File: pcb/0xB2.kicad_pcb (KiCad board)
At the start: 2 copper layers, 17.8 x 33 mm, 42 parts, among them J1 USB_C_Receptacle_USB2.0, J2 Conn_01x12, J3 Conn_01x05, J4 Conn_01x12, J5 Conn_01x02, SW1 SW_Push, SW2 SW_Push, U1 RP2040, U2 GD25Q80CEIGR, U3 XC6210B332MR-G, Y1 Crystal_GND24

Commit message: import
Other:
- board size 17.8 x 33 mm -> 41.8 x 50.8 mm
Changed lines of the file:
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@@
       (xy 149.2 92.45)
     ) (layer "F.SilkS") (width 0.15) (fill solid))
-  (gr_line (start 143.51 107.95) (end 143.51 77.47) (layer "Edge.Cuts") (width 0.1))
-  (gr_line (start 148.05 81.35) (end 149.25 81.35) (layer "Edge.Cuts") (width 0.1))
-  (gr_arc (start 155.55 81.75) (mid 155.491421 81.891421) (end 155.35 81.95) (layer "Edge.Cuts") (width 0.1))
-  (gr_line (start 156.95 81.15) (end 156.95 76.2) (layer "Edge.Cuts") (width 0.1))
-  (gr_arc (start 161.29 107.95) (mid 160.918026 108.848026) (end 160.02 109.22) (layer "Edge.Cuts") (width 0.1))
-  (gr_line (start 147.85 76.2) (end 147.85 81.15) (layer "Edge.Cuts") (width 0.1))
-  (gr_arc (start 144.78 109.22) (mid 143.881974 108.848026) (end 143.51 107.95) (layer "Edge.Cuts") (width 0.1))
-  (gr_arc (start 156.95 81.15) (mid 156.891421 81.291421) (end 156.75 81.35) (layer "Edge.Cuts") (width 0.1))
-  (gr_line (start 149.25 81.35) (end 149.25 81.75) (layer "Edge.Cuts") (width 0.1))
-  (gr_line (start 161.29 77.47) (end 161.29 107.95) (layer "Edge.Cuts") (width 0.1))
-  (gr_line (start 160.02 109.22) (end 144.78 109.22) (layer "Edge.Cuts") (width 0.1))
-  (gr_line (start 144.78 76.2) (end 147.85 76.2) (layer "Edge.Cuts") (width 0.1))
-  (gr_line (start 155.55 81.75) (end 155.55 81.35) (layer "Edge.Cuts") (width 0.1))
-  (gr_arc (start 149.45 81.95) (mid 149.308579 81.891421) (end 149.25 81.75) (layer "Edge.Cuts") (width 0.1))
-  (gr_line (start 156.95 76.2) (end 160.02 76.2) (layer "Edge.Cuts") (width 0.1))
-  (gr_arc (start 148.05 81.35) (mid 147.908579 81.291421) (end 147.85 81.15) (layer "Edge.Cuts") (width 0.1))
-  (gr_arc (start 160.02 76.2) (mid 160.918026 76.571974) (end 161.29 77.47) (layer "Edge.Cuts") (width 0.1))
-  (gr_line (start 155.55 81.35) (end 156.75 81.35) (layer "Edge.Cuts") (width 0.1))
-  (gr_arc (start 143.51 77.47) (mid 143.881974 76.571974) (end 144.78 76.2) (layer "Edge.Cuts") (width 0.1))
-  (gr_line (start 149.45 81.95) (end 155.35 81.95) (layer "Edge.Cuts") (width 0.1))
+  (gr_arc (start 150.323649 128.768354) (mid 149.285 128.335) (end 148.86165 127.292233) (layer "Edge.Cuts") (width 0.2))
+  (gr_arc (start 174.953514 106.488749) (mid 177.10863 111.211774) (end 173.011529 114.400074) (layer "Edge.Cuts") (width 0.2))
+  (gr_line (start 161.993697 78.84806) (end 138.649352 78.809096) (layer "Edge.Cuts") (width 0.2))
+  (gr_line (start 171.173514 77.998749) (end 163.855 78.015) (layer "Edge.Cuts") (width 0.2))
+  (gr_arc (start 162.955 78.415) (mid 163.367804 78.13131) (end 163.855 78.015) (layer "Edge.Cuts") (width 0.1))
+  (gr_line (start 150.323649 128.768354) (end 165.179642 128.797362) (layer "Edge.Cuts") (width 0.2))
+  (gr_arc (start 174.953514 106.488749) (mid 173.241074 104.864213) (end 172.613514 102.588749) (layer "Edge.Cuts") (width 0.2))
+  (gr_arc (start 135.454058 82.315) (mid 136.31466 79.890303) (end 138.649352 78.809096) (layer "Edge.Cuts") (width 0.2))
+  (gr_arc (start 166.652176 127.348393) (mid 166.216517 128.378374) (end 165.179642 128.797362) (layer "Edge.Cuts") (width 0.2))
+  (gr_line (start 148.885 113.835) (end 148.858709 117.290003) (layer "Edge.Cuts") (width 0.1))
+  (gr_line (start 141.724995 91.687466) (end 141.724995 96.446645) (layer "Edge.Cuts") (width 0.1))
+  (gr_arc (start 138.908049 87.137466) (mid 140.993806 88.993153) (end 141.724995 91.687466) (layer "Edge.Cuts") (width 0.2))
+  (gr_arc (start 144.085 110.835) (mid 142.403633 109.806429) (end 141.785 107.935) (layer "Edge.Cuts") (width 0.1))
+  (gr_arc (start 171.173514 77.998749) (mid 172.200088 78.436278) (end 172.623514 79.468749) (layer "Edge.Cuts") (width 0.2))
+  (gr_arc (start 145.956134 110.835) (mid 147.980525 111.788319) (end 148.885 113.835) (layer "Edge.Cuts") (width 0.1))
+  (gr_arc (start 138.908049 87.137466) (mid 136.390014 85.292799) (end 135.454058 82.315) (layer "Edge.Cuts") (width 0.2))
+  (gr_line (start 166.641051 116.931051) (end 166.652176 127.348393) (layer "Edge.Cuts") (width 0.2))
+  (gr_arc (start 166.641051 116.931051) (mid 167.385 115.135) (end 169.181051 114.391051) (layer "Edge.Cuts") (width 0.2))
+  (gr_line (start 148.86165 127.292233) (end 148.858709 117.290003) (layer "Edge.Cuts") (width 0.1))
+  (gr_line (start 141.724995 96.446645) (end 141.785 107.935) (layer "Edge.Cuts") (width 0.1))
+  (gr_arc (start 162.955 78.415) (mid 162.522461 78.738329) (end 161.993697 78.84806) (layer "Edge.Cuts") (width 0.1))
+  (gr_line (start 172.613514 102.588749) (end 172.623514 79.468749) (layer "Edge.Cuts") (width 0.2))
+  (gr_line (start 145.956134 110.835) (end 144.085 110.835) (layer "Edge.Cuts") (width 0.1))
+  (gr_line (start 169.181051 114.391051) (end 173.011529 114.400074) (layer "Edge.Cuts") (width 0.2))
   (gr_text "v2" (at 148.9 105.35) (layer "B.SilkS")
     (effects (font (size 0.6 0.6) (thickness 0.15)) (justify mirror))

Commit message: import libs
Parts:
- added H1: M4, Library:MountingHole_4mm_Pad_thin, F.Cu at (138.7, 82.1)
- added H2: M4, Library:MountingHole_4mm_Pad_thin, F.Cu at (173.2, 110.0)
- added J6: Ribbon, Library:6_PinHeader, F.Cu at (161.7, 114.2)
- added J7: Ribbon, Library:5_PinHeader, F.Cu at (156.8, 114.2)
- added kibuzzard-61F01940: G***, kibuzzard-61F01940, F.Cu at (159.3, 111.2)
- added kibuzzard-61F01940: G***, kibuzzard-61F01940, B.Cu at (159.3, 111.2)
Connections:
- net /A0 renamed row2_r
- net /A1 renamed col1_r
- net /A2 renamed col2_r
- net /A3 renamed row1_r
- net /D21 renamed col3_r
- net /D4 renamed row4_r
- net /D5 renamed row3_r
- net /D6 renamed col4_r
- net /D7 renamed col5_r
- net /D8 renamed col6_r
- net /D9 renamed row5_r
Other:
- board text added: "C1"
- board text added: "C2"
- board text added: "C3"
- board text added: "C4"
- board text added: "C5"
- board text added: "C6"
- board text added: "R1"
- board text added: "R2"
- board text added: "R3"
- board text added: "R4"
- board text added: "R5"

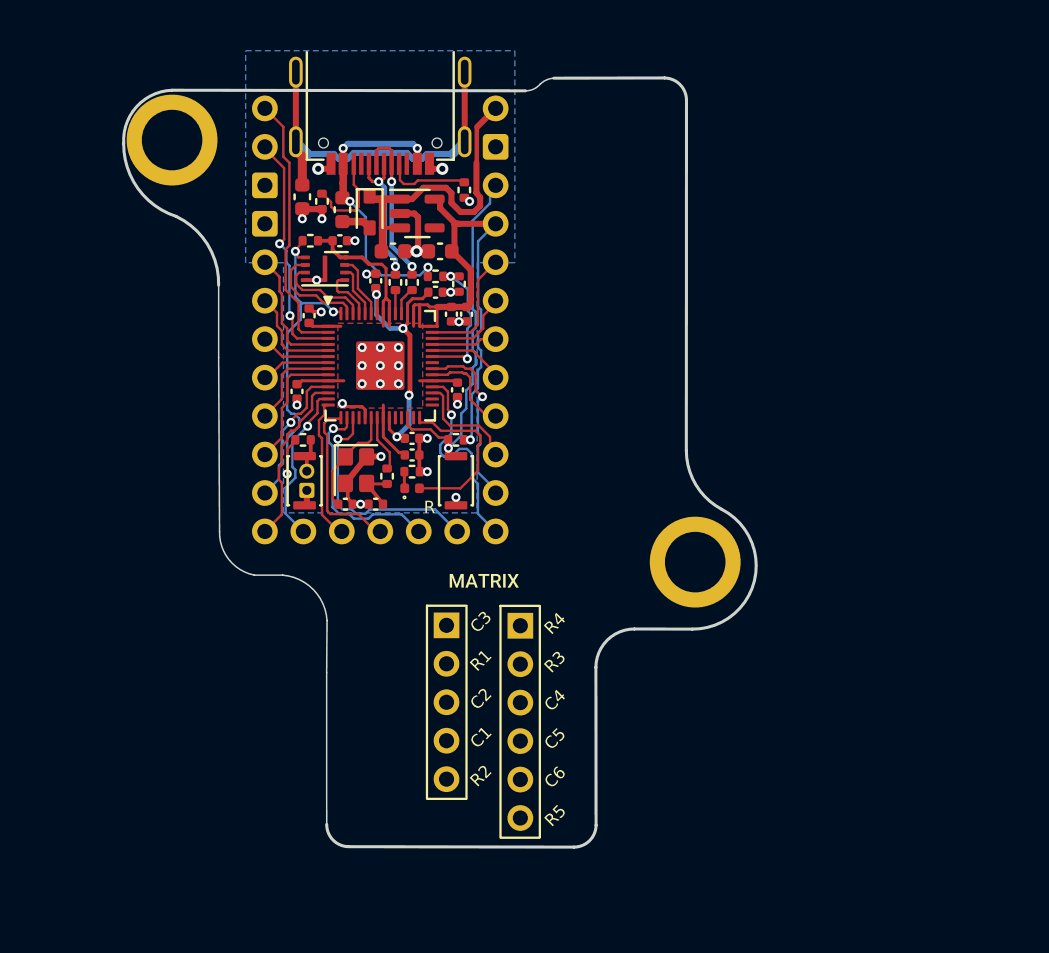
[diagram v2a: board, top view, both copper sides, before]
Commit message: add new and remove old connectors
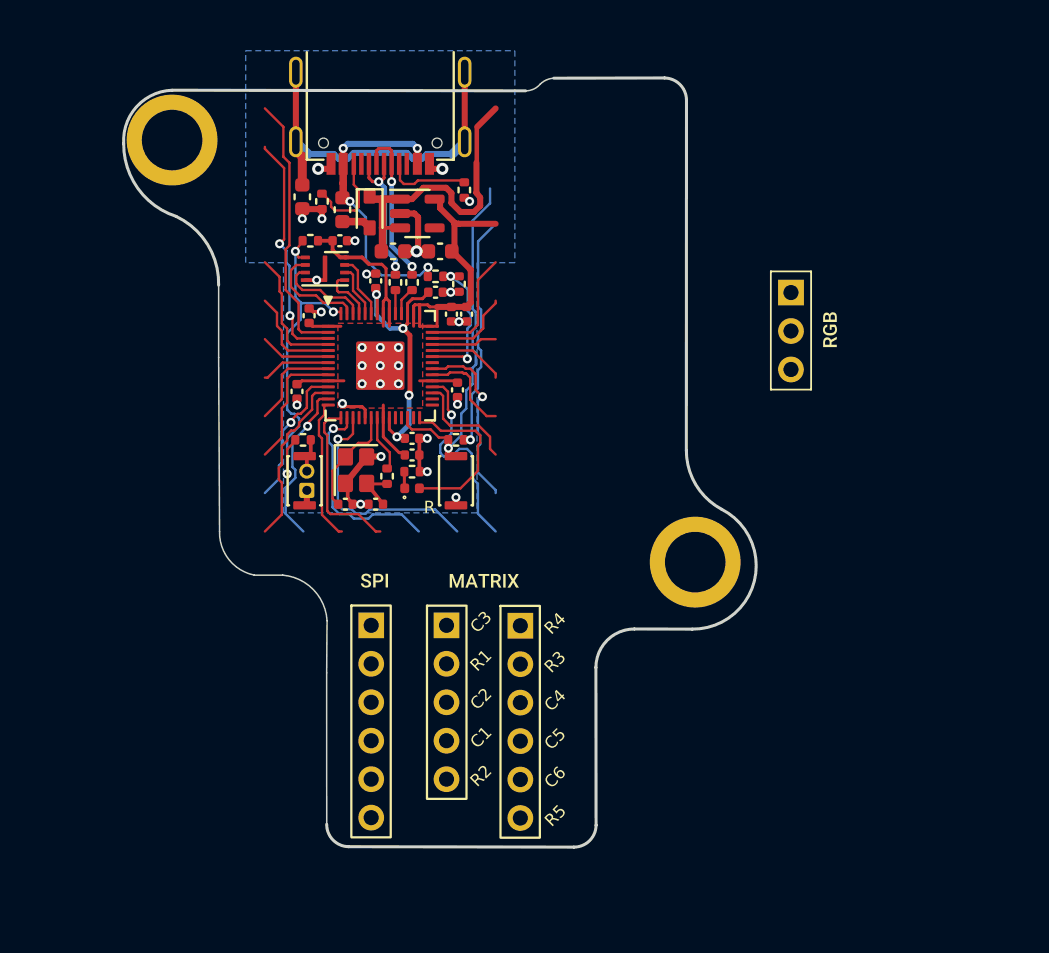
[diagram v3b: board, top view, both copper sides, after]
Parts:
- removed J2, J4: Conn_01x12, 0xLib_Connectors:PinHeader_1x12_P2.54mm
- removed J3: Conn_01x05, 0xLib_Connectors:PinHeader_1x05_P2.54mm
- added J10: RGB, Library:header1x03, F.Cu at (179.5, 92.2)
- added J8: trackball, Library:6_PinHeader, F.Cu at (151.8, 114.2)
- added kibuzzard-61F01957: G***, kibuzzard-61F01957, F.Cu at (152.0, 111.2)
- added kibuzzard-61F01957: G***, kibuzzard-61F01957, B.Cu at (152.1, 111.2)
- added kibuzzard-61F019CB: G***, kibuzzard-61F019CB, F.Cu at (182.1, 94.6)
- added kibuzzard-61F019CB: G***, kibuzzard-61F019CB, B.Cu at (182.1, 94.7)
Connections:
- net col1_r renamed /A1
- net col2_r renamed /A2
- net col3_r renamed /D21
- net col4_r renamed /D6
- net col5_r renamed /D7
- net col6_r renamed /D8
- net row1_r renamed /A3
- net row2_r renamed /A0
- net row3_r renamed /D5
- net row4_r renamed /D4
- net row5_r renamed /D9

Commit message: add reversible reset button
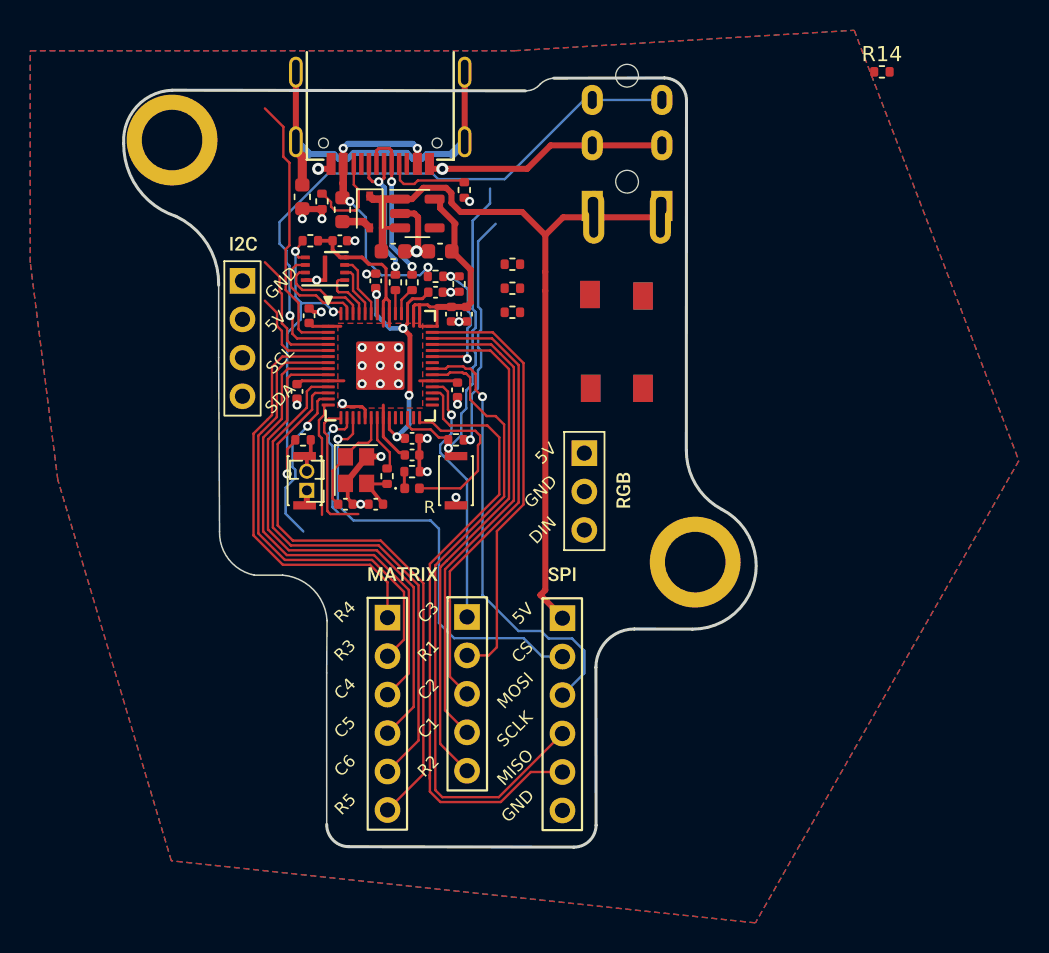
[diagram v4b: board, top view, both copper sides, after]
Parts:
- added J11: serial, Library:PinHeader_1x04_P2.54mm_Vertical, F.Cu at (143.3, 91.4)
- added J9: Serial, Library:Jack_3.5mm_PJ320E_Horizontal, B.Cu at (171.0, 86.5)
- added R12: 4.7k, Resistor_SMD:R_0402_1005Metric, F.Cu at (161.1, 93.5)
- added R13: 4.7k, Resistor_SMD:R_0402_1005Metric, F.Cu at (161.1, 91.9)
- added R14: 5.1k, Resistor_SMD:R_0402_1005Metric, F.Cu at (185.5, 77.6)
- added R14: 5.1k, Resistor_SMD:R_0402_1005Metric, F.Cu at (161.1, 90.3)
- added SW3: SW_SPST, Library:PushSwitch, F.Cu at (168.1, 95.4)
- added kibuzzard-620B8D91: G***, kibuzzard-620B8D91, F.Cu at (143.4, 88.9)
- added kibuzzard-620B8D91: G***, kibuzzard-620B8D91, B.Cu at (143.4, 88.9)
- moved J10 17.3 mm to (165.9, 102.8)
- moved kibuzzard-61F019CB 17.3 mm to (168.4, 105.2)
- moved kibuzzard-61F019CB 17.3 mm to (168.4, 105.3)
- moved J8 12.6 mm to (164.4, 113.7)
- moved kibuzzard-61F01957 12.4 mm to (164.4, 110.8)
- moved kibuzzard-61F01957 12.4 mm to (164.5, 110.8)
- moved J6 8.79 mm to (152.9, 113.6)
- moved kibuzzard-61F01940 5.39 mm to (153.9, 110.8) (x2)
- moved J7 1.46 mm to (158.1, 113.6)
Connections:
- J10 pad 3: rgb_r -> /D0
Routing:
- net /SCLK: track 6.29 -> 43.4 mm
- net /MISO: track 7.22 -> 41.9 mm
- net +5V: track 20.5 -> 52.4 mm
- net /A0: track 5.08 -> 34.7 mm
- net /A1: track 4.33 -> 32.6 mm
- net /D7: track 8.44 -> 34.9 mm
- net /D6: track 6.42 -> 32.8 mm
- net /D8: track 9.51 -> 35.8 mm, vias 1 -> 0
- net /D5: track 4.59 -> 30.8 mm
- net /D9: track 11.7 -> 37.8 mm
- net /A2: track 5.80 -> 30.5 mm
- net /D4: track 4.66 -> 28.1 mm
- net /D1: track 15.9 -> 39.2 mm, vias 2 -> 1
- net /A3: track 7.83 -> 28.5 mm
- net /MOSI: track 11.9 -> 29.7 mm
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- added copper zone on F.Cu, net GND
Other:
- board text added: "5V"
- board text added: "CS"
- board text added: "DIN"
- board text added: "GND"
- board text added: "MISO"
- board text added: "MOSI"
- board text added: "SCL"
- board text added: "SCLK"
- board text added: "SDA"

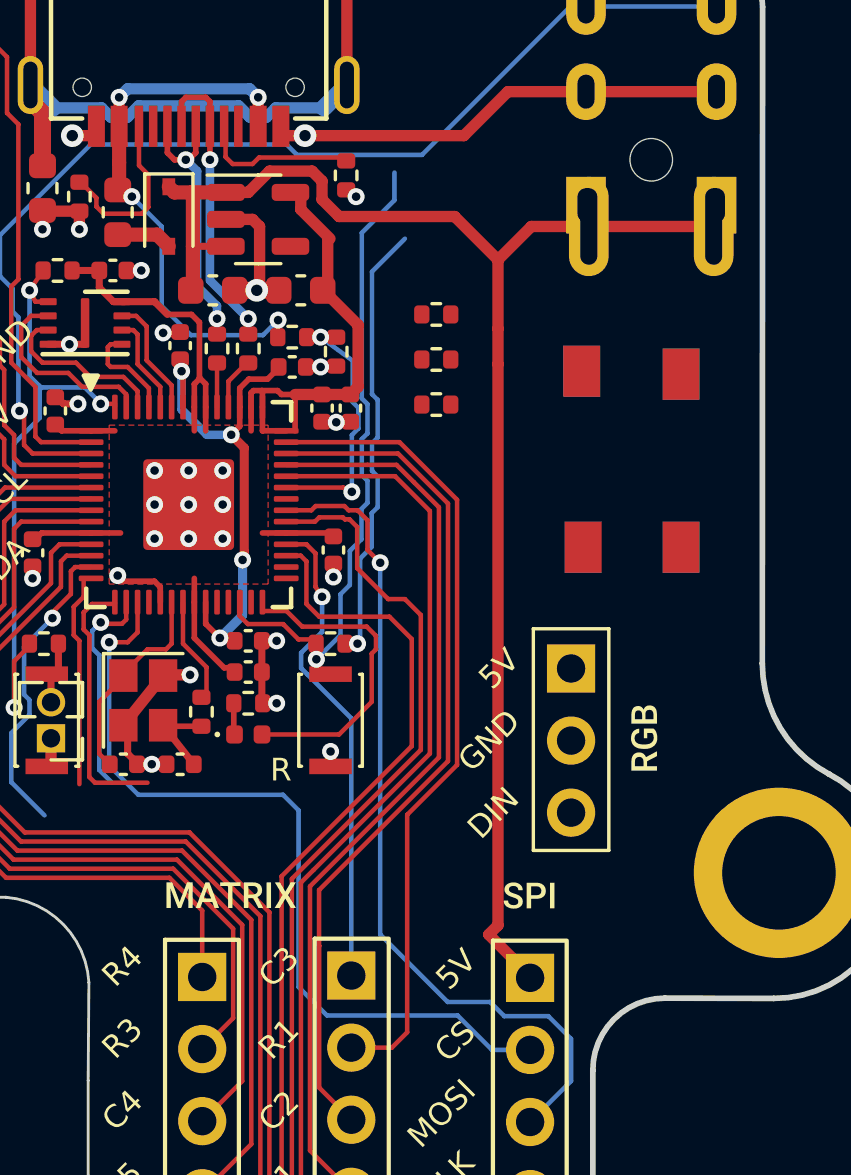
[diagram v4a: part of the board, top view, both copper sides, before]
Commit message: remove small reset button
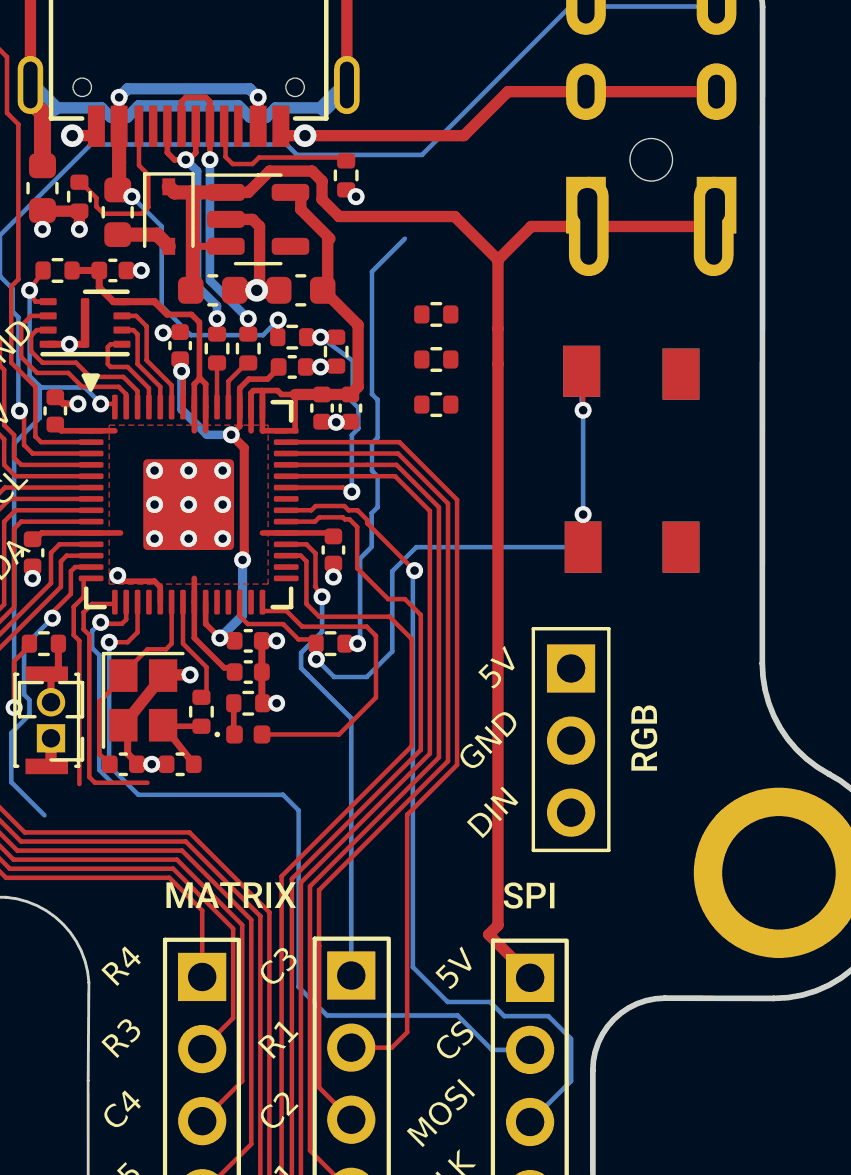
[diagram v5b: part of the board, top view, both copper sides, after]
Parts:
- removed SW1: SW_Push, Button_Switch_SMD:SW_SPST_CK_KXT3
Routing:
- net /~{RESET}: track 24.9 -> 26.7 mm, vias 1 -> 3
- net GND: track 45.1 -> 44.6 mm, vias 29 -> 28

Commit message: routing
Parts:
- removed the R14 at (161.1, 90.3)
- moved R12 15.8 mm to (145.4, 91.5), turned to 90 degrees
- moved R13 15.8 mm to (145.5, 94.0), turned to -90 degrees
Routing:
- net /D0: track 17.8 -> 56.5 mm, vias 0 -> 2
- net /D10: track 10.9 -> 0.00 mm, vias 1 -> 0
- net /D12: track 9.30 -> 0.00 mm
- net /D3: track 6.58 -> 14.7 mm, vias 0 -> 1
- net /D11: track 7.74 -> 0.00 mm
- net /D13: track 7.66 -> 0.00 mm, vias 1 -> 0
- net /D2: track 8.60 -> 12.5 mm, vias 0 -> 1
- net +3V3: track 56.4 -> 52.8 mm, vias 1 -> 2
- net +5V: track 52.4 -> 55.5 mm
- net /VBUS_DET: track 9.59 -> 11.5 mm
- net /D1: track 39.2 -> 37.7 mm
- net /MOSI: track 29.7 -> 30.4 mm
- net /QSPI_~{CS}: track 23.0 -> 22.4 mm
